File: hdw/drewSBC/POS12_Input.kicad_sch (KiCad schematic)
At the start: 30 parts

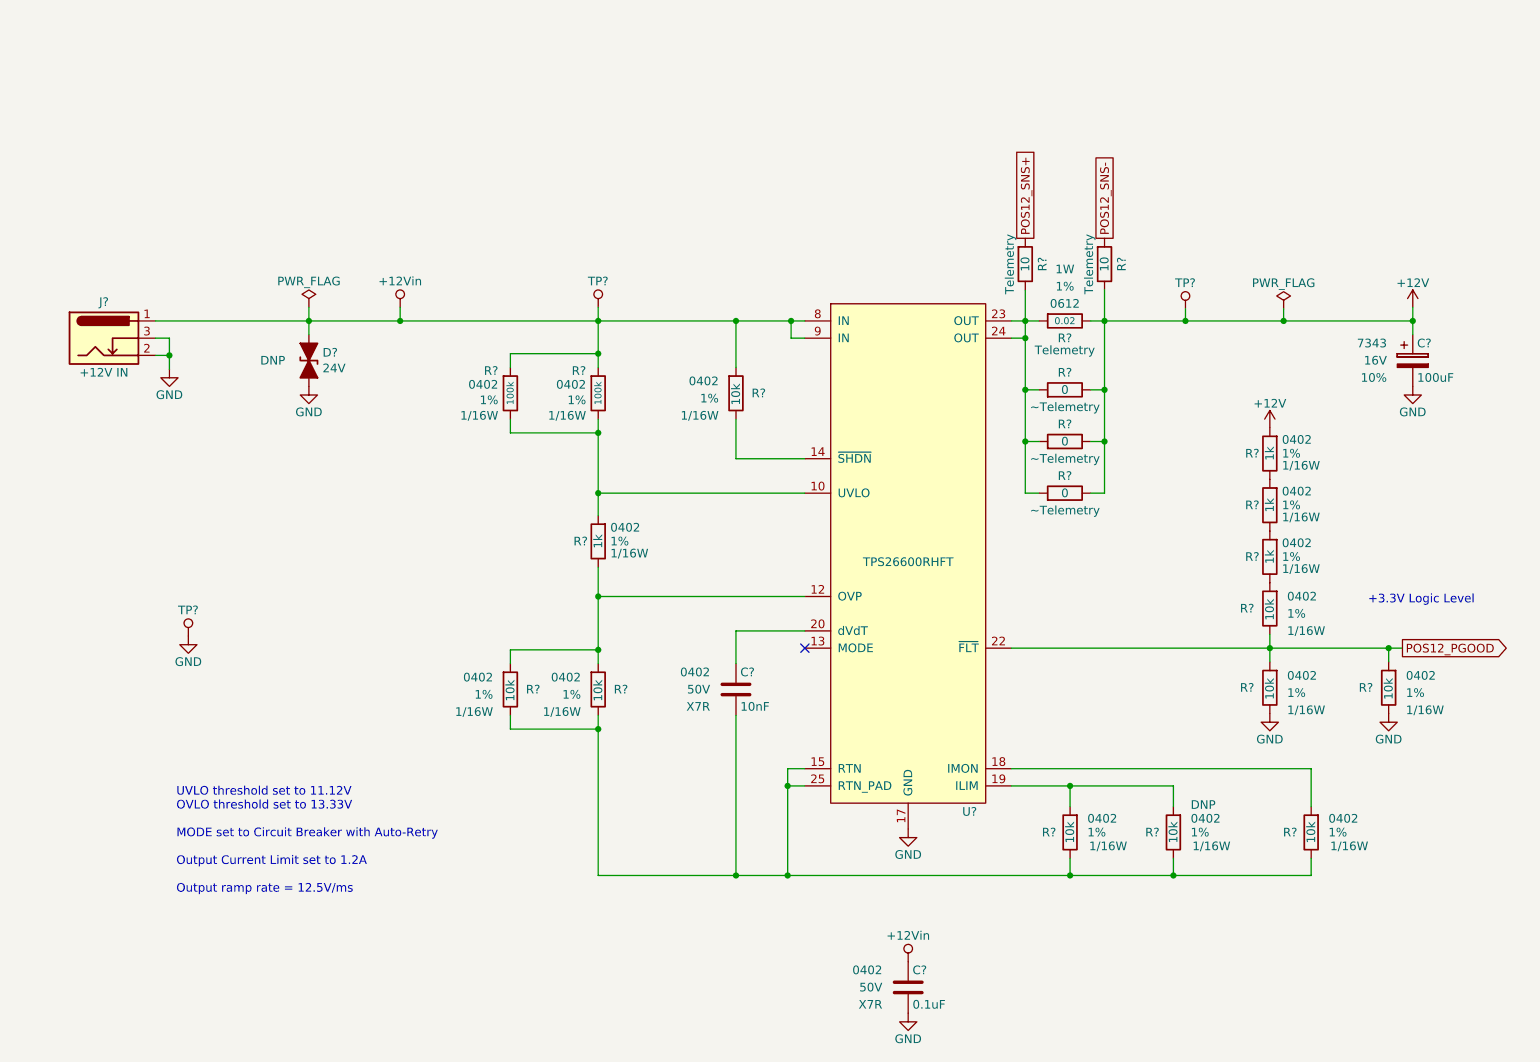
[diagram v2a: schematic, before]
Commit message: ripped up ETH phy
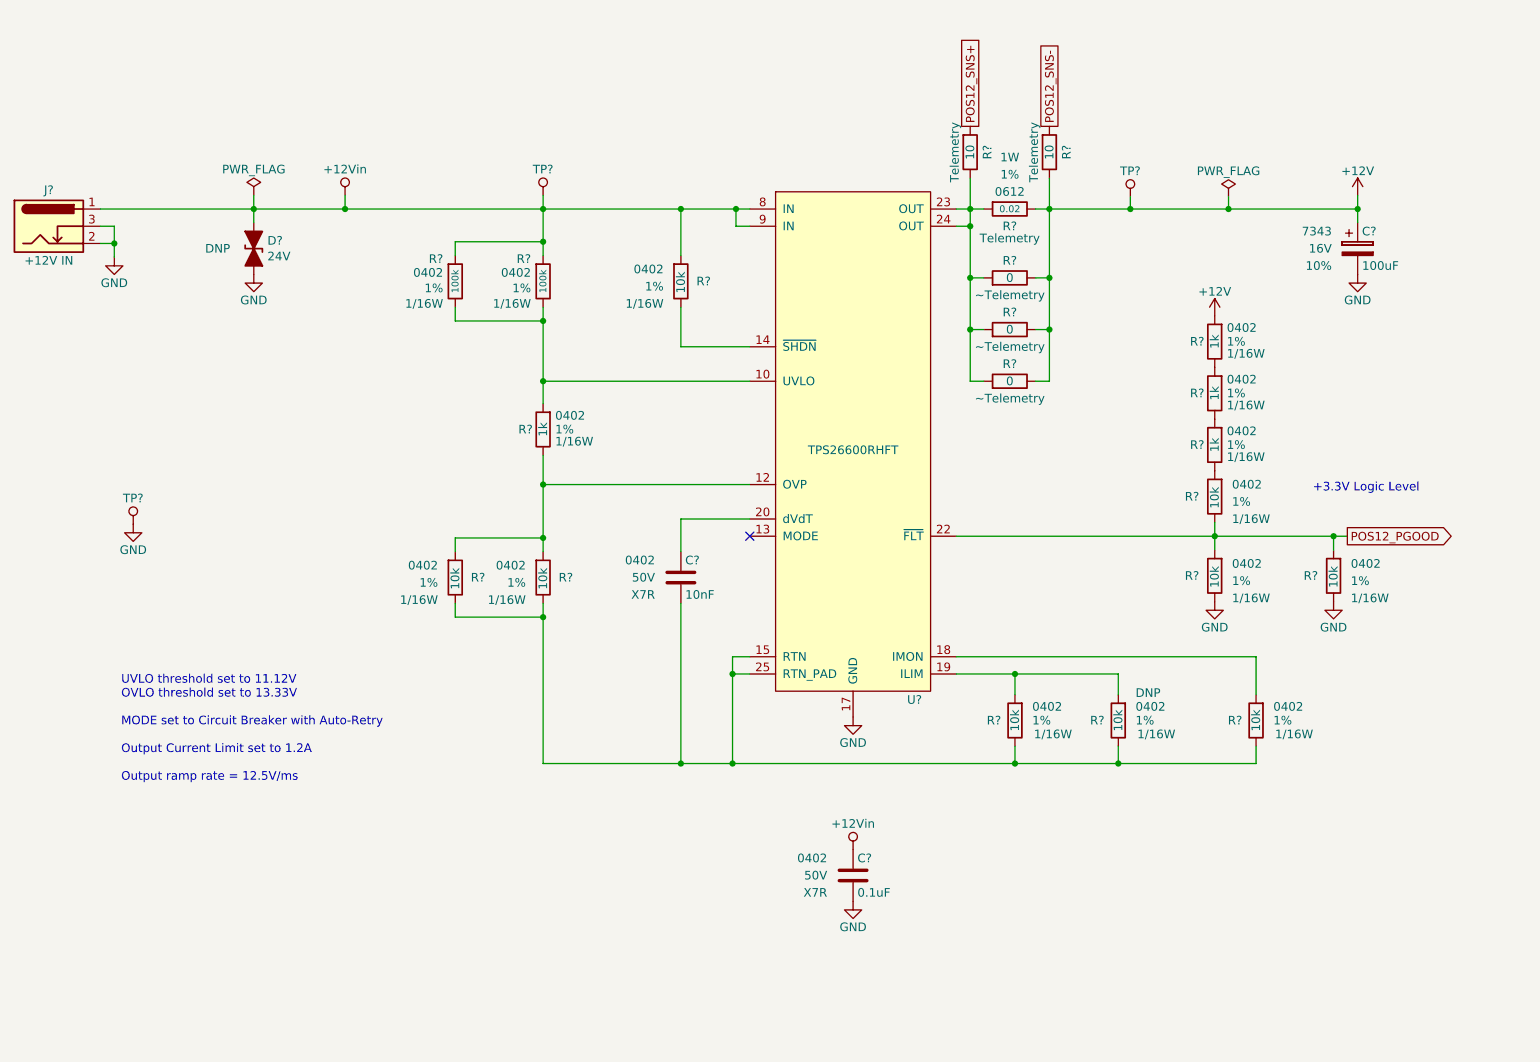
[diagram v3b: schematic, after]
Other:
- moved on the sheet: C?, D?, J?, R?, TP?, U?
